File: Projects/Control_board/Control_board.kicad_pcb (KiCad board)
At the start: 2 copper layers, 48 parts, among them IC1 BD1HD500FVM-CTR, J1 505567-0681, J2 43045-0200, J3 43045-0200, J4 43045-0200, J5 43045-0401, J6 Conn_01x06, J8 Conn_01x02, K3 PB114024, Q1 BSS138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

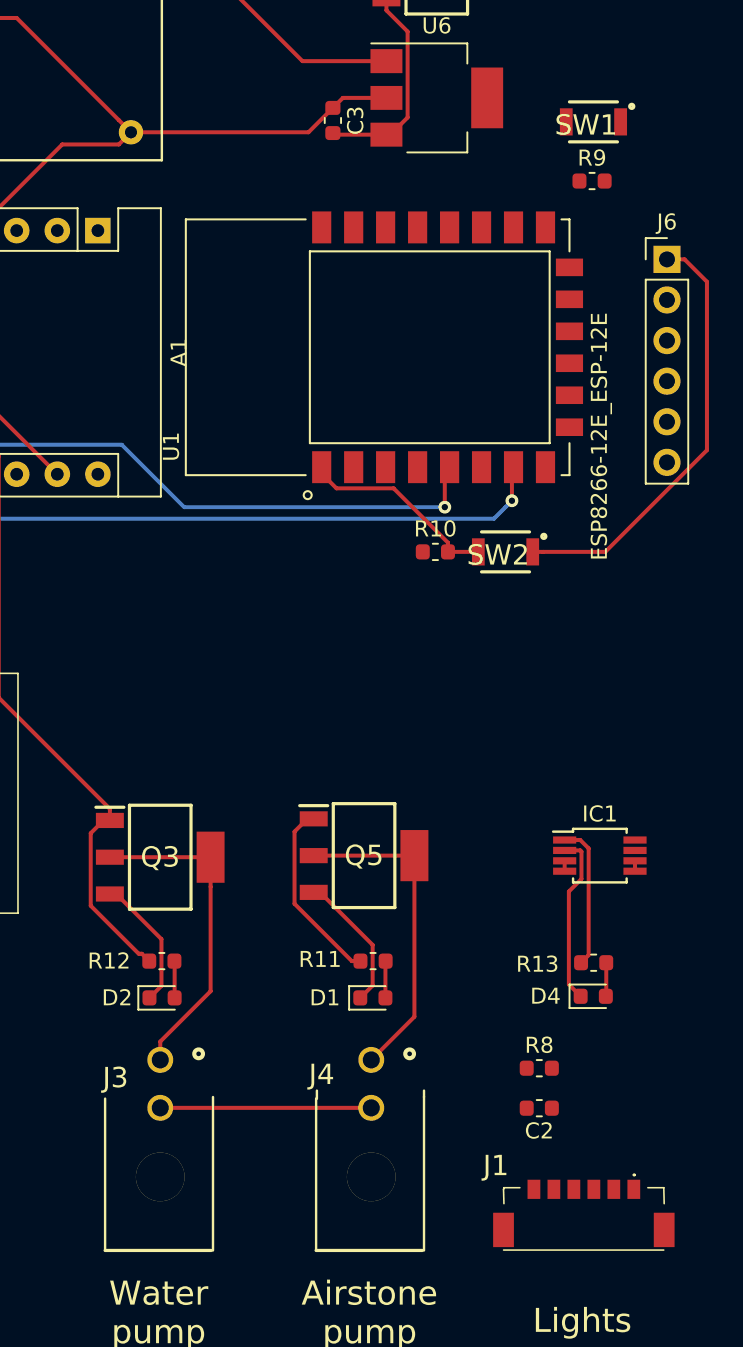
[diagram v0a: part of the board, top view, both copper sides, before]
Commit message: added LED with fan project
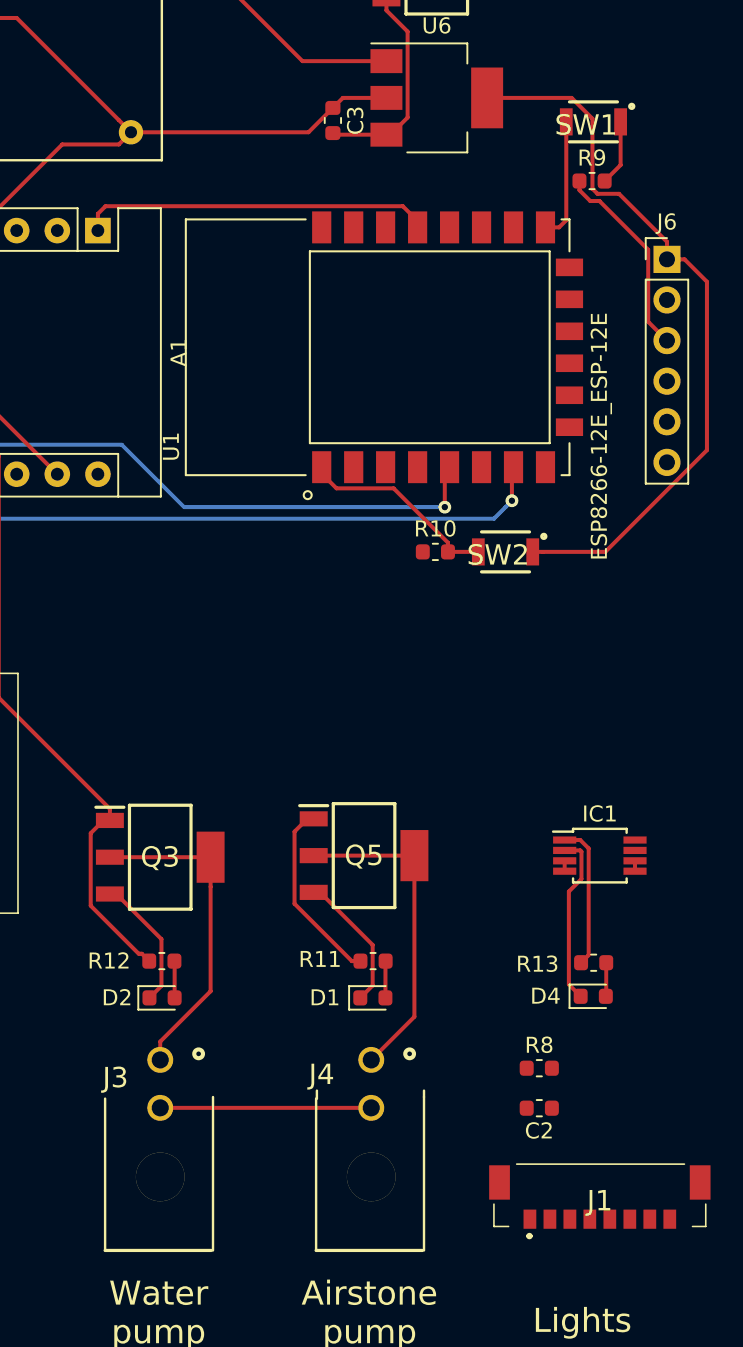
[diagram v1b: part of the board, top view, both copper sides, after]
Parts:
- J1: value 505567-0681 -> 505567-0871; footprint SamacSys_Parts:5055670681 -> 5055670871
- moved J1 1.22 mm to (159.8, 171.9), turned to 0 degrees
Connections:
- A1 pad 21: /Temp_data_3V3 -> /NTC
- A1 pad 25: /mistmaker -> (no net)
- A1 pad 26: /NTC -> (no net)
- A1 pad 5: (no net) -> /mistmaker
- A1 pad 6: (no net) -> /Temp_data_3V3
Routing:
- net /fan: track 9.06 -> 31.1 mm
- net GND: track 278.4 -> 297.0 mm
- net +3V3: track 59.8 -> 72.4 mm
- net Net-(SW1-Pad2): track 0.00 -> 7.64 mm
- net Net-(R9-Pad2): track 0.00 -> 4.11 mm

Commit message: added pca96...
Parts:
- removed SW1, SW2: SW_Push, SamacSys_Parts:B3U-1000P
- removed U1: ESP8266-12E_ESP-12E, ESP8266-12E_ESP-12E:XCVR_ESP8266-12E%2fESP-12E
- removed U3: LM1117-3.3, SamacSys_Parts:SOT230P700X180-4N
- added C5: 1uF, Capacitor_SMD:C_0603_1608Metric, F.Cu at (196.2, 116.4)
- added IC2: PCA9615DPJ, SamacSys_Parts:QFN50P300X300X100-10N-D, F.Cu at (149.1, 113.9)
- added R15: 10K, Resistor_SMD:R_0603_1608Metric, F.Cu at (164.7, 163.5)
- added R16: 390, Resistor_SMD:R_0603_1608Metric, F.Cu at (182.5, 135.1)
- added R17: 100, Resistor_SMD:R_0603_1608Metric, F.Cu at (196.2, 120.9)
- added R18: 390, Resistor_SMD:R_0603_1608Metric, F.Cu at (199.2, 117.9)
- C4: value 1uF -> 0.1uF
- J1: value 505567-0871 -> 5055780871; footprint 5055670871 -> footprints:5055780871
- J6: value Conn_01x06 -> RJ45; footprint Connector_PinHeader_2.54mm:PinHeader_1x06_P2.54mm_Vertical -> Connector_RJ:RJ45_Amphenol_54602-x08_Horizontal
- R10, R3: value 10k -> 390
- R9: value 10k -> 100
- moved C4 53.8 mm to (179.5, 135.1), turned to 0 degrees
- moved R10 48.2 mm to (196.2, 119.4)
- moved R3 45.8 mm to (199.2, 116.4)
- moved R9 38.1 mm to (196.2, 117.9)
- moved J6 6.57 mm to (167.6, 118.5), turned to 90 degrees
- moved C2 3.60 mm to (158.5, 163.5)
- moved R8 1.41 mm to (154.6, 163.5)
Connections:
- A1 pad 25: (no net) -> /mistmaker
- A1 pad 26: (no net) -> /pump
- A1 pad 5: /mistmaker -> /EN
- A1 pad 9: /pump -> (no net)
- C4 pad 1: GND -> +3V3
- C4 pad 2: +3V3 -> GND
- J1 pad 2: (no net) -> /ADJ_LED
- J1 pad 3: (no net) -> GND
- J1 pad 4: (no net) -> +36V
- J1 pad 6: +36V -> (no net)
- J1 pad 7: GND -> (no net)
- J1 pad 8: /ADJ_LED -> +3V3
- J6 pad 1: GND -> /DSCL-
- J6 pad 2: (no net) -> /DSCL+
- J6 pad 3: +3V3 -> (no net)
- J6 pad 4: /TXO -> +3V3
- J6 pad 5: /RXI -> GND
- R10 pad 1: +3V3 -> /DSDA-
- R10 pad 2: Net-(R10-Pad2) -> GND
- R3 pad 1: +3V3 -> +5V
- R3 pad 2: Net-(R3-Pad2) -> /DSDA+
- R5 pad 1: +5V -> +3V3
- R7 pad 1: +5V -> +3V3
- R9 pad 1: +3V3 -> /DSDA+
- R9 pad 2: Net-(R9-Pad2) -> /DSDA-
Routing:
- net +36V: track 32.0 -> 187.8 mm
- net /ADJ: track 0.00 -> 83.5 mm
- net /NTC: track 39.8 -> 104.0 mm, vias 1 -> 0
- net /LDR: track 106.4 -> 54.3 mm, vias 2 -> 0
- net /fan: track 31.1 -> 63.0 mm, vias 0 -> 1
- net /Temp_data_3V3: track 34.7 -> 3.77 mm
- net Net-(A1-Pad23): track 4.25 -> 28.5 mm, vias 0 -> 1
- net (no net): track 0.00 -> 20.8 mm
- net /pump: track 56.8 -> 37.3 mm
- net +5V: track 68.0 -> 53.9 mm
- net Net-(R10-Pad2): track 12.6 -> 0.00 mm
- net /fan_status: track 0.00 -> 11.4 mm, vias 0 -> 1
- net /ADJ_LED: track 0.00 -> 10.3 mm
- net GND: track 297.0 -> 287.1 mm, vias 0 -> 6
- net +3V3: track 72.4 -> 63.6 mm
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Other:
- net class 36volt added: clearance 1, trace_width 1, via_dia 0.8, via_drill 0.4

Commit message: updates to Control board and LED light
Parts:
- moved C5 51.6 mm to (144.7, 112.5), turned to 270 degrees
- moved R3 50.5 mm to (151.0, 101.2), turned to 270 degrees
- moved R18 48.5 mm to (151.0, 112.1), turned to 90 degrees
- moved C4 47.2 mm to (137.3, 114.1), turned to 270 degrees
- moved R9 47.1 mm to (151.0, 104.4), turned to 270 degrees
- moved R10 46.7 mm to (151.0, 107.6), turned to 270 degrees
- moved R17 45.5 mm to (151.0, 115.4), turned to 90 degrees
- moved R16 35.6 mm to (151.0, 118.7), turned to 90 degrees
- moved U6 9.67 mm to (139.9, 102.3)
- moved J6 9.30 mm to (159.2, 114.5)
- moved C3 8.59 mm to (134.6, 103.5)
- moved IC2 7.91 mm to (141.2, 114.3)
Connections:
- C1 pad 1: Net-(C1-Pad1) -> +3V3
- IC1 pad 3: /fan_+12V -> /12V_Fan
- IC1 pad 4: /fan_+12V -> /12V_Fan
- J1 pad 7: (no net) -> /12V_Fan
- U2 pad 8: Net-(C1-Pad1) -> +3V3
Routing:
- net GND: track 287.1 -> 518.7 mm
- net +3V3: track 63.6 -> 230.9 mm, vias 0 -> 4
- net +12V: track 76.5 -> 235.5 mm, vias 0 -> 1
- net +5V: track 53.9 -> 181.9 mm, vias 0 -> 3
- net +24V: track 13.1 -> 139.5 mm
- net Net-(A1-Pad24): track 3.88 -> 77.7 mm, vias 0 -> 2
- net /fan_status: track 11.4 -> 68.3 mm, vias 1 -> 2
- net /Temp_data_3V3: track 3.77 -> 54.8 mm, vias 0 -> 1
- net Net-(A1-Pad23): track 28.5 -> 76.8 mm, vias 1 -> 2
- net /airstone_pump: track 14.8 -> 55.8 mm, vias 0 -> 1
- net /EN: track 0.00 -> 27.8 mm
- net /DSDA+: track 0.00 -> 26.1 mm, vias 0 -> 1
- net /DSCL-: track 0.00 -> 25.7 mm
- net /12V_Fan: track 0.00 -> 23.6 mm, vias 0 -> 2
- net /DSDA-: track 0.00 -> 23.5 mm
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- added copper zone on F.Cu, net GND
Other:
- board outline added: 97.1 x 121.5 mm
- net class Power added: clearance 0.2, trace_width 1, via_dia 0.8, via_drill 0.4
- net class Power_2 added: clearance 0.2, trace_width 0.5, via_dia 0.8, via_drill 0.4
- board text added: "24V DC"
- board text added: "5V DC airstone"
- board text added: "5V DC pump"
- board text removed: "24V DC MistM."
- board text removed: "Airstone pump"
- board text removed: "Water pump"

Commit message: ready for production:)
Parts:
- added REF**: MountingHole_3.2mm_M3, MountingHole:MountingHole_3.2mm_M3, F.Cu at (169.0, 156.0)
- added REF**: MountingHole_3.2mm_M3, MountingHole:MountingHole_3.2mm_M3, F.Cu at (84.0, 177.0)
- added REF**: MountingHole_3.2mm_M3, MountingHole:MountingHole_3.2mm_M3, F.Cu at (169.0, 68.0)
- added REF**: MountingHole_3.2mm_M3, MountingHole:MountingHole_3.2mm_M3, F.Cu at (84.2, 68.0)
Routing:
- net +12V: track 235.5 -> 220.7 mm
- net +3V3: track 230.9 -> 234.2 mm
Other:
- board text added: "+"
- board text added: "-"
- board text added: "12V+"
- board text added: "24V+"
- board text added: "36V"
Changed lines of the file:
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@@
-(kicad_pcb (version 20171130) (host pcbnew "(5.1.2)-2")
+(kicad_pcb (version 20171130) (host pcbnew "(5.1.4)-1")
   (general
     (thickness 1.6)
-    (drawings 12)
-    (tracks 509)
+    (drawings 17)
+    (tracks 516)
     (zones 0)
-    (modules 50)
+    (modules 54)
     (nets 38)
   )
@@
       (outputformat 1)
       (mirror false)
-      (drillshape 1)
+      (drillshape 0)
       (scaleselection 1)
-      (outputdirectory ""))
+      (outputdirectory "../../FABRICATION/"))
   )
   (net 0 "")
@@
     (add_net /pump)
   )
+  (module MountingHole:MountingHole_3.2mm_M3 (layer F.Cu)
+    (at 169 156)
+    (descr "Mounting Hole 3.2mm, no annular, M3")
+    (tags "mounting hole 3.2mm no annular m3")
+    (attr virtual)
+    (fp_text reference REF** (at 0 -4.2) (layer F.SilkS) hide
+      (effects (font (size 1 1) (thickness 0.15)))
+    )
+    (fp_text value MountingHole_3.2mm_M3 (at 0 4.2) (layer F.Fab)
+      (effects (font (size 1 1) (thickness 0.15)))
+    )
+    (fp_circle (center 0 0) (end 3.45 0) (layer F.CrtYd) (width 0.05))
+    (fp_circle (center 0 0) (end 3.2 0) (layer Cmts.User) (width 0.15))
+    (fp_text user %R (at 0.3 0) (layer F.Fab) hide
+      (effects (font (size 1 1) (thickness 0.15)))
+    )
+    (pad 1 np_thru_hole circle (at 0 0) (size 3.2 3.2) (drill 3.2) (layers *.Cu *.Mask))
+  )
+  (module MountingHole:MountingHole_3.2mm_M3 (layer F.Cu)
+    (at 84 177)
+    (descr "Mounting Hole 3.2mm, no annular, M3")
+    (tags "mounting hole 3.2mm no annular m3")
+    (attr virtual)
+    (fp_text reference REF** (at 0 -4.2) (layer F.SilkS) hide
+      (effects (font (size 1 1) (thickness 0.15)))
+    )
+    (fp_text value MountingHole_3.2mm_M3 (at 0 4.2) (layer F.Fab)
+      (effects (font (size 1 1) (thickness 0.15)))
+    )
+    (fp_circle (center 0 0) (end 3.45 0) (layer F.CrtYd) (width 0.05))
+    (fp_circle (center 0 0) (end 3.2 0) (layer Cmts.User) (width 0.15))
+    (fp_text user %R (at 0.3 0) (layer F.Fab) hide
+      (effects (font (size 1 1) (thickness 0.15)))
+    )
+    (pad 1 np_thru_hole circle (at 0 0) (size 3.2 3.2) (drill 3.2) (layers *.Cu *.Mask))
+  )
+  (module MountingHole:MountingHole_3.2mm_M3 (layer F.Cu)
+    (at 169 68)
+    (descr "Mounting Hole 3.2mm, no annular, M3")
+    (tags "mounting hole 3.2mm no annular m3")
+    (attr virtual)
+    (fp_text reference REF** (at 0 -4.2) (layer F.SilkS) hide
+      (effects (font (size 1 1) (thickness 0.15)))
+    )
+    (fp_text value MountingHole_3.2mm_M3 (at 0 4.2) (layer F.Fab)
+      (effects (font (size 1 1) (thickness 0.15)))
+    )
+    (fp_text user %R (at 0.3 0) (layer F.Fab) hide
+      (effects (font (size 1 1) (thickness 0.15)))
+    )
+    (fp_circle (center 0 0) (end 3.2 0) (layer Cmts.User) (width 0.15))
+    (fp_circle (center 0 0) (end 3.45 0) (layer F.CrtYd) (width 0.05))
+    (pad 1 np_thru_hole circle (at 0 0) (size 3.2 3.2) (drill 3.2) (layers *.Cu *.Mask))
+  )
+  (module MountingHole:MountingHole_3.2mm_M3 (layer F.Cu)
+    (at 84.2 68)
+    (descr "Mounting Hole 3.2mm, no annular, M3")
+    (tags "mounting hole 3.2mm no annular m3")
+    (attr virtual)
+    (fp_text reference REF** (at 0 -4.2) (layer F.SilkS) hide
+      (effects (font (size 1 1) (thickness 0.15)))
+    )
+    (fp_text value MountingHole_3.2mm_M3 (at 0 4.2) (layer F.Fab)
+      (effects (font (size 1 1) (thickness 0.15)))
+    )
+    (fp_circle (center 0 0) (end 3.45 0) (layer F.CrtYd) (width 0.05))
+    (fp_circle (center 0 0) (end 3.2 0) (layer Cmts.User) (width 0.15))
+    (fp_text user %R (at 0.3 0) (layer F.Fab) hide
+      (effects (font (size 1 1) (thickness 0.15)))
+    )
+    (pad 1 np_thru_hole circle (at 0 0) (size 3.2 3.2) (drill 3.2) (layers *.Cu *.Mask))
+  )
   (module footprints:5055780871 (layer F.Cu)
     (at 159.8 171.9)
@@
     (tags connector)
     (attr virtual)
-    (fp_text reference J8 (at 3.175 -3.81 90) (layer F.SilkS)
+    (fp_text reference J8 (at 3.175 -3.81 90) (layer F.SilkS) hide
       (effects (font (size 1 1) (thickness 0.15)))
     )
@@
       (net 16 +5V))
   )
+  (gr_text 24V+ (at 114 62.5) (layer F.SilkS)
+    (effects (font (size 1 1) (thickness 0.15)))
+  )
+  (gr_text 12V+ (at 91 62.5) (layer F.SilkS)
+    (effects (font (size 1 1) (thickness 0.15)))
+  )
+  (gr_text - (at 79.5 95.5) (layer F.SilkS)
+    (effects (font (size 2 2) (thickness 0.3)))
+  )
+  (gr_text + (at 79.5 102) (layer F.SilkS)
+    (effects (font (size 2 2) (thickness 0.3)))
+  )
+  (gr_text 36V (at 84 91) (layer F.SilkS)
+    (effects (font (size 2 2) (thickness 0.3)))
+  )
   (gr_line (start 78.2 182.9) (end 78.3 182.9) (layer Edge.Cuts) (width 0.15))
   (gr_line (start 78.1 182.9) (end 78.2 182.9) (layer Edge.Cuts) (width 0.15))
@@
   (gr_line (start 174.8 183) (end 175.2 61.6) (layer Edge.Cuts) (width 0.15))
   (gr_line (start 174.8 183) (end 78.3 182.9) (layer Edge.Cuts) (width 0.15))
-  (gr_text Lights (at 158.7 179.4) (layer F.SilkS)
+  (gr_text Lights (at 162 180) (layer F.SilkS)
     (effects (font (size 1.5 1.5) (thickness 0.3)))
   )
@@
   (segment (start 120.2 120.6) (end 119.800001 120.999999) (width 0.25) (layer B.Cu) (net 2))
   (segment (start 119.236411 120.999999) (end 114.285001 125.951409) (width 0.25) (layer B.Cu) (net 2))
-  (segment (start 169.8 168.488) (end 169.8 132.6) (width 0.25) (layer F.Cu) (net 2))
   (segment (start 157.9 120.7) (end 155.085002 120.7) (width 0.25) (layer F.Cu) (net 2))
-  (segment (start 169.8 132.6) (end 157.9 120.7) (width 0.25) (layer F.Cu) (net 2))
   (segment (start 152.0175 85.1125) (end 151.9 84.995) (width 0.25) (layer F.Cu) (net 2) (status 30))
   (segment (start 154.2 85.1125) (end 152.0175 85.1125) (width 0.25) (layer F.Cu) (net 2) (status 30))
@@
   (segment (start 162.56 93.4725) (end 162.56 108.42) (width 0.25) (layer F.Cu) (net 2))
   (segment (start 154.2 85.1125) (end 162.56 93.4725) (width 0.25) (layer F.Cu) (net 2))
+  (segment (start 170.55 168.488) (end 173 166.038) (width 0.25) (layer F.Cu) (net 2))
+  (segment (start 169.8 168.488) (end 170.55 168.488) (width 0.25) (layer F.Cu) (net 2))
+  (segment (start 173 135.8) (end 169.6 132.4) (width 0.25) (layer F.Cu) (net 2))
+  (segment (start 173 166.038) (end 173 135.8) (width 0.25) (layer F.Cu) (net 2))
+  (segment (start 169.8 132.6) (end 169.6 132.4) (width 0.25) (layer F.Cu) (net 2))
+  (segment (start 169.6 132.4) (end 157.9 120.7) (width 0.25) (layer F.Cu) (net 2))
   (segment (start 145.475 88.805) (end 145.18 89.1) (width 0.25) (layer F.Cu) (net 3))
   (segment (start 146.5 88.805) (end 145.475 88.805) (width 0.25) (layer F.Cu) (net 3) (status 10))
@@
   (segment (start 161.9 151) (end 162.234315 151) (width 0.5) (layer F.Cu) (net 25))
   (segment (start 162.234315 151) (end 162.434315 151.2) (width 0.5) (layer F.Cu) (net 25))
-  (segment (start 90.73 65.55) (end 93.65 65.55) (width 0.5) (layer B.Cu) (net 25))
-  (segment (start 93.65 65.55) (end 96 63.2) (width 0.5) (layer B.Cu) (net 25))
-  (segment (start 96 63.2) (end 166.2 63.2) (width 0.5) (layer B.Cu) (net 25))
-  (segment (start 166.2 63.2) (end 172.8 69.8) (width 0.5) (layer B.Cu) (net 25))
   (via (at 162.7 151.9) (size 0.8) (drill 0.4) (layers F.Cu B.Cu) (net 25))
-  (segment (start 172.8 69.8) (end 172.8 141.8) (width 0.5) (layer B.Cu) (net 25))
-  (segment (start 172.8 141.8) (end 162.7 151.9) (width 0.5) (layer B.Cu) (net 25))
   (segment (start 162.234315 151.434315) (end 162.234315 151) (width 0.5) (layer F.Cu) (net 25))
   (segment (start 162.7 151.9) (end 162.234315 151.434315) (width 0.5) (layer F.Cu) (net 25))
+  (segment (start 172.8 141.8) (end 162.7 151.9) (width 0.5) (layer B.Cu) (net 25))
+  (segment (start 172.8 99.8) (end 172.8 141.8) (width 0.5) (layer B.Cu) (net 25))
+  (segment (start 131.573762 82) (end 155 82) (width 0.5) (layer B.Cu) (net 25))
+  (segment (start 155 82) (end 172.8 99.8) (width 0.5) (layer B.Cu) (net 25))
+  (segment (start 90.73 65.55) (end 93.28 63) (width 0.5) (layer B.Cu) (net 25))
+  (segment (start 93.28 63) (end 117 63) (width 0.5) (layer B.Cu) (net 25))
+  (segment (start 117 63) (end 128 74) (width 0.5) (layer B.Cu) (net 25))
+  (segment (start 128 78.426238) (end 131.573762 82) (width 0.5) (layer B.Cu) (net 25))
+  (segment (start 128 74) (end 128 78.426238) (width 0.5) (layer B.Cu) (net 25))
   (segment (start 128.75 148.1) (end 129.15 148.1) (width 0.25) (layer F.Cu) (net 26) (status 30))
   (segment (start 127.949999 148.900001) (end 128.75 148.1) (width 0.25) (layer F.Cu) (net 26) (status 20))

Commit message: minor changes
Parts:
- removed D4: LED, LED_SMD:LED_0603_1608Metric
- removed IC1: BD1HD500FVM-CTR, Package_SO:MSOP-8_3x3mm_P0.65mm
- removed R13: 1k, Resistor_SMD:R_0603_1608Metric
- removed REF** (x4): MountingHole_3.2mm_M3, MountingHole:MountingHole_3.2mm_M3
- C2: footprint Capacitor_SMD:C_0603_1608Metric -> Capacitor_SMD:C_1206_3216Metric
- IC2: footprint SamacSys_Parts:QFN50P300X300X100-10N-D -> Package_SO:TSSOP-10_3x3mm_P0.5mm
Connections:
- A1 pad 1: /fan -> (no net)
- A1 pad 14: (no net) -> /pump
- A1 pad 15: (no net) -> /fan
- A1 pad 22: /ADJ -> (no net)
- A1 pad 25: /mistmaker -> (no net)
- A1 pad 26: /pump -> (no net)
- A1 pad 8: /fan_status -> (no net)
- A1 pad 9: (no net) -> /ADJ
- J2 pad 1: Net-(J2-Pad1) -> /12V_Fan
- K3 pad 14: Net-(J2-Pad1) -> /12V_Fan
- Q4 pad 1: /mistmaker -> /fan
- R14 pad 1: /mistmaker -> /fan
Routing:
- net +12V: track 220.7 -> 61.1 mm, vias 1 -> 0
- net /fan_status: track 68.3 -> 0.00 mm, vias 2 -> 0
- net /pump: track 37.3 -> 89.6 mm, vias 0 -> 1
- net /12V_Fan: track 23.6 -> 73.8 mm
- net /mistmaker: track 36.6 -> 0.00 mm
- net Net-(J2-Pad1): track 15.9 -> 0.00 mm
- net +5V: track 181.9 -> 195.9 mm
- net /ADJ: track 83.5 -> 94.7 mm, vias 0 -> 1
- net GND: track 518.7 -> 509.0 mm
- net /fan: track 63.0 -> 56.9 mm
- net Net-(D4-Pad2): track 2.11 -> 0.00 mm
